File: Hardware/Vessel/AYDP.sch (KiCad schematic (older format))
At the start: 5 parts

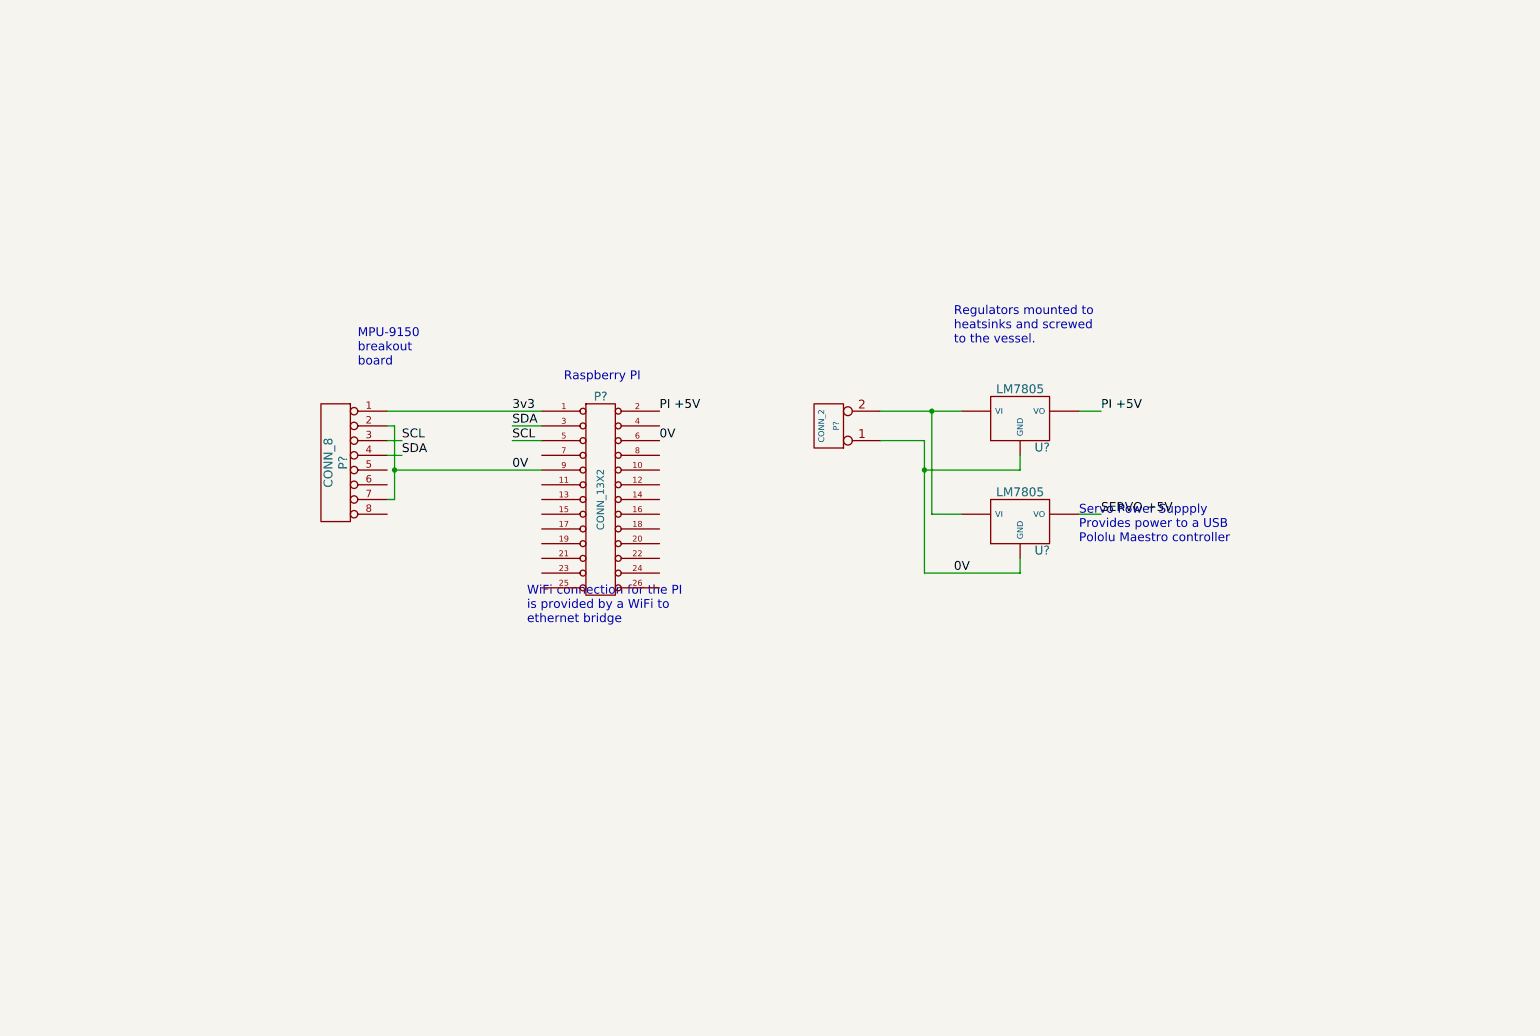
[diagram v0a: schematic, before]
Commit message: Major cleanup of directory structure
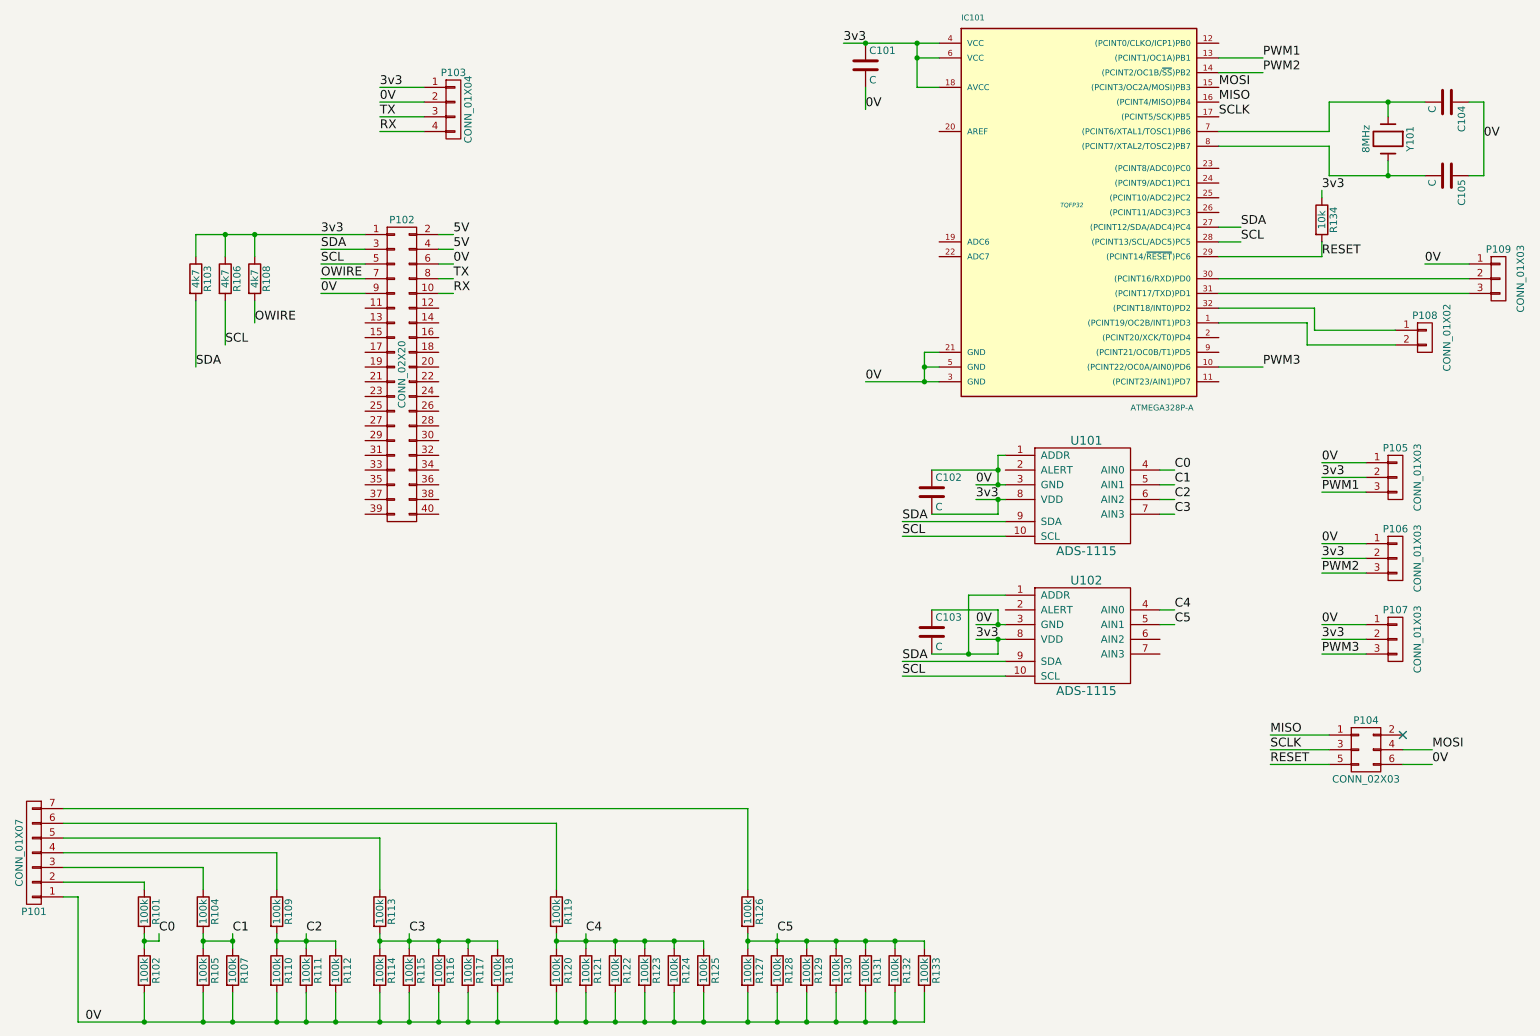
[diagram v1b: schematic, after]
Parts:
- removed P?: CONN_13X2, symbol CONN_13X2
- removed P?: CONN_2, symbol CONN_2
- removed P?: CONN_8, symbol CONN_8
- removed U? (x2): LM7805, symbol LM7805
- added C101, C102, C103, C104, C105: C, symbol C
- added IC101: ATMEGA328P-A, TQFP32, symbol ATMEGA328P-A
- added P101: CONN_01X07, symbol CONN_01X07
- added P102: CONN_02X20, symbol CONN_02X20
- added P103: CONN_01X04, symbol CONN_01X04
- added P104: CONN_02X03, symbol CONN_02X03
- added P105, P106, P107, P109: CONN_01X03, symbol CONN_01X03
- added P108: CONN_01X02, symbol CONN_01X02
- added R101, R102, R104, R105, R107, R109, R110, R111, R112, R113, R114, R115, R116, R117, R118, R119, R120, R121, R122, R123, R124, R125, R126, R127, R128, R129, R130, R131, R132, R133: 100k, symbol R
- added R103, R106, R108: 4k7, symbol R
- added R134: 10k, symbol R
- added U101, U102: ADS-1115, symbol ADS-1115
- added Y101: 8MHz, symbol Crystal
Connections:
- net 0V: now also C101.2, C102.1, C103.1, C104.1, C105.1, IC101.21 (GND), IC101.3 (GND), IC101.5 (GND), P101.1 (P1), P102.6 (P6), P102.9 (P9), P103.2 (P2), P104.6 (P6), P105.1 (P1), P106.1 (P1), P107.1 (P1), P109.1 (P1), R102.2, R105.2, R107.2, R110.2, R111.2, R112.2, R114.2, R115.2, R116.2, R117.2, R118.2, R120.2, R121.2, R122.2, R123.2, R124.2, R125.2, R127.2, R128.2, R129.2, R130.2, R131.2, R132.2, R133.2, U101.1 (ADDR), U101.3 (GND), U102.3 (GND)
- net 3v3: now also C101.1, C102.2, C103.2, IC101.18 (AVCC), IC101.4 (VCC), IC101.6 (VCC), P102.1 (P1), P103.1 (P1), P105.2 (P2), P106.2 (P2), P107.2 (P2), R103.1, R106.1, R108.1, R134.1, U101.8 (VDD), U102.1 (ADDR), U102.8 (VDD)
- net SCL: now also IC101.28 ((PCINT13/SCL/ADC5)PC5), P102.5 (P5), R106.2, U101.10 (SCL), U102.10 (SCL)
- net SDA: now also IC101.27 ((PCINT12/SDA/ADC4)PC4), P102.3 (P3), R103.2, U101.9 (SDA), U102.9 (SDA)
- new net: IC101.1 ((PCINT19/OC2B/INT1)PD3), P108.2 (P2)
- new net: IC101.30 ((PCINT16/RXD)PD0), P109.2 (P2)
- new net: IC101.31 ((PCINT17/TXD)PD1), P109.3 (P3)
- new net: IC101.32 ((PCINT18/INT0)PD2), P108.1 (P1)
- new net: C104.2, IC101.7 ((PCINT6/XTAL1/TOSC1)PB6), Y101.1
- new net: C105.2, IC101.8 ((PCINT7/XTAL2/TOSC2)PB7), Y101.2
- new net: P101.2 (P2), R101.1
- new net: P101.3 (P3), R104.1
- new net: P101.4 (P4), R109.1
- new net: P101.5 (P5), R113.1
- new net: P101.6 (P6), R119.1
- new net: P101.7 (P7), R126.1
- new net 5V: P102.2 (P2), P102.4 (P4)
- new net C0: R101.2, R102.1, U101.4 (AIN0)
- new net C1: R104.2, R105.1, R107.1, U101.5 (AIN1)
- new net C2: R109.2, R110.1, R111.1, R112.1, U101.6 (AIN2)
- new net C3: R113.2, R114.1, R115.1, R116.1, R117.1, R118.1, U101.7 (AIN3)
- new net C4: R119.2, R120.1, R121.1, R122.1, R123.1, R124.1, R125.1, U102.4 (AIN0)
- new net C5: R126.2, R127.1, R128.1, R129.1, R130.1, R131.1, R132.1, R133.1, U102.5 (AIN1)
- new net MISO: IC101.16 ((PCINT4/MISO)PB4), P104.1 (P1)
- new net MOSI: IC101.15 ((PCINT3/OC2A/MOSI)PB3), P104.4 (P4)
- new net OWIRE: P102.7 (P7), R108.2
- new net PWM1: IC101.13 ((PCINT1/OC1A)PB1), P105.3 (P3)
- new net PWM2: IC101.14 ((PCINT2/OC1B/~SS~)PB2), P106.3 (P3)
- new net PWM3: IC101.10 ((PCINT22/OC0A/AIN0)PD6), P107.3 (P3)
- new net RESET: IC101.29 ((PCINT14/~RESET~)PC6), P104.5 (P5), R134.2
- new net RX: P102.10 (P10), P103.4 (P4)
- new net SCLK: IC101.17 ((PCINT5/SCK)PB5), P104.3 (P3)
- new net TX: P102.8 (P8), P103.3 (P3)
- no-connect marks 0 -> 1
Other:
- note removed: "MPU-9150\nbreakout\nboard"
- note removed: "Raspberry PI"
- note removed: "Regulators mounted to\nheatsinks and screwed\nto the vessel."
- note removed: "Servo Power Suppply\nProvides power to a USB\nPololu Maestro controller"
- note removed: "WiFi connection for the PI\nis provided by a WiFi to\nethernet bridge"
